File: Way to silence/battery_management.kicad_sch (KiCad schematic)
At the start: 9 parts, among them U2 SM5308

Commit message: [DRC] Working on BMS Sheet
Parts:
- added C10: C, symbol Way to silence:C
- added C11, C12, C13, C15, C16: 22uF, symbol Way to silence:C
- added C14: 4.7nF, symbol Way to silence:C
- added C9: 10uF, symbol Way to silence:C
- added L1: 1UH, symbol Way to silence:L
- added R16: 0.5R, symbol Way to silence:R
- added R17: 1R, symbol Way to silence:R
- added R18: 0.1R, symbol Way to silence:R
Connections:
- net GND: now also C10.2, C11.2, C12.2, C13.2, C14.2, C15.1, C16.1, C9.2
- net VIN: now reaches U2.1 (VIN)
- net VIN: now also C9.1, R16.1
- net at U2.6 (BAT): now also C16.2, R18.1
- net at U2.7 (SW): now also L1.1, R17.1
- net VOUT: now reaches U2.8 (VOUT)
- net VOUT: now also C11.1, C12.1, C13.1
- new net: C14.1, R17.2
- new net: C10.1, R16.2
- new net BAT: C15.2, L1.2, R18.2
- no-connect marks 0 -> 1

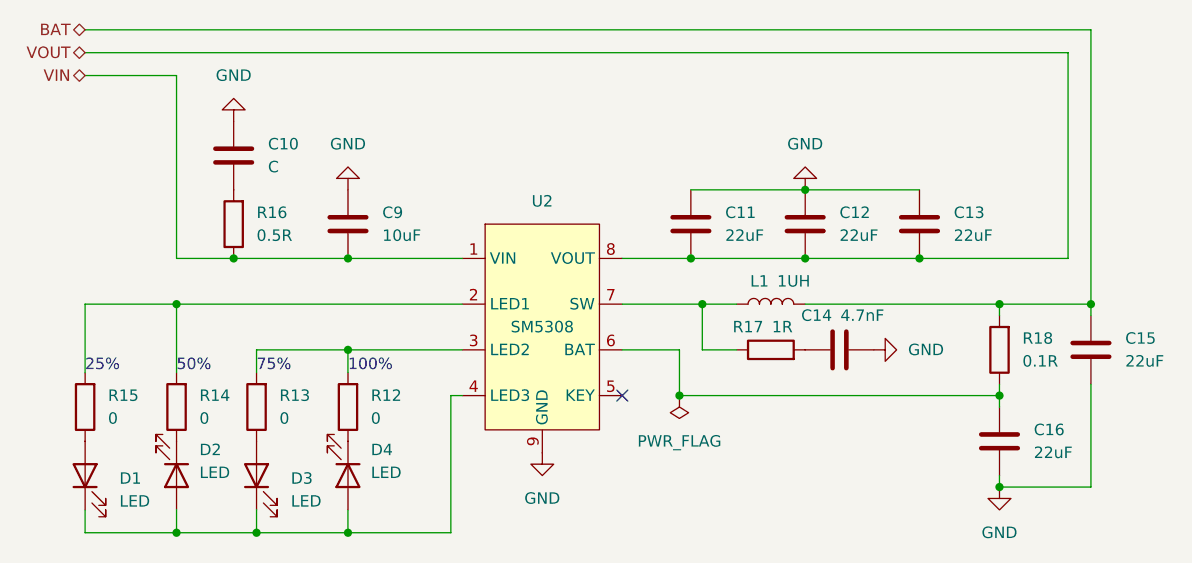
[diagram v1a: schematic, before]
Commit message: [ADD] LSCS Parts and Footprints for BMS
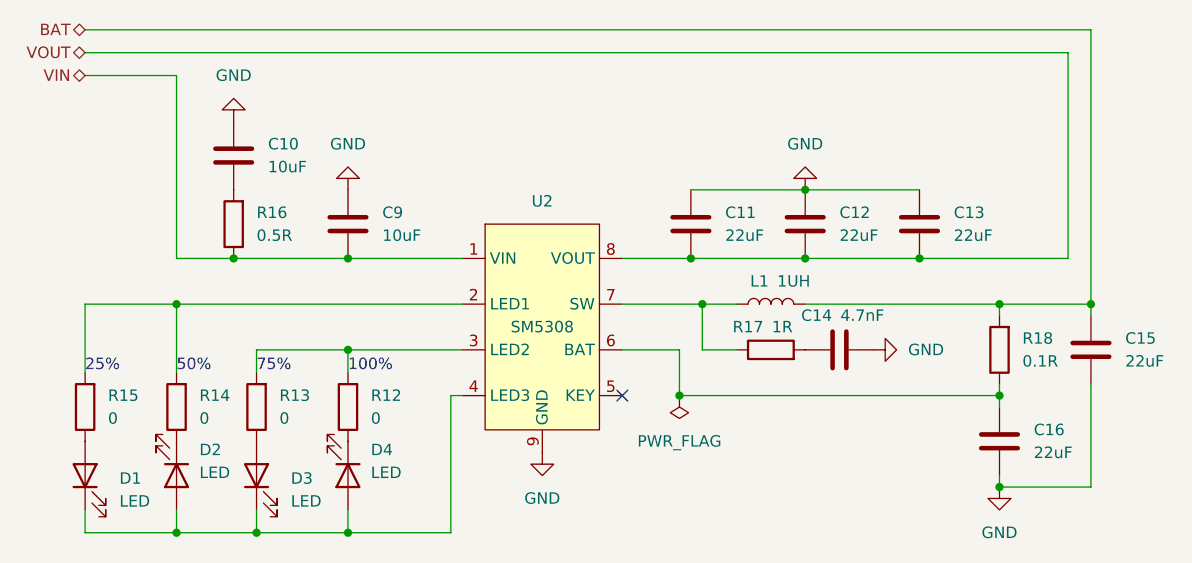
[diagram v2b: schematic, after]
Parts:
- C10: value C -> 10uF; footprint (none) -> Way to silence:C_0603_1608Metric; LCSC (none) -> C77041
- C11, C12, C13, C15, C16: footprint (none) -> Way to silence:C_0603_1608Metric; LCSC (none) -> C59461
- C14: footprint (none) -> Way to silence:C_0603_1608Metric
- C9: footprint (none) -> Way to silence:C_0603_1608Metric; LCSC (none) -> C77041
- D1, D2, D3, D4: footprint (none) -> Way to silence:LED_0603; LCSC (none) -> C84263
- R12, R13, R14, R15: footprint (none) -> Way to silence:R_0603_1608Metric; LCSC (none) -> C21189
- R16: footprint (none) -> Way to silence:R_0603_1608Metric; LCSC (none) -> C2934253
- R17: footprint (none) -> Way to silence:R_0603_1608Metric; LCSC (none) -> C25212
- R18: footprint (none) -> Way to silence:R_0603_1608Metric; LCSC (none) -> C705486
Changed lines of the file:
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@@
       (effects (font (size 1.27 1.27)) (justify right))
     )
-    (property "Footprint" "" (at 27.178 59.69 0)
+    (property "Footprint" "Way to silence:R_0603_1608Metric" (at 27.178 59.69 0)
       (effects (font (size 1.27 1.27)) hide)
     )
     (property "Datasheet" "~" (at 25.4 59.69 90)
+      (effects (font (size 1.27 1.27)) hide)
+    )
+    (property "LCSC" "C21189" (at 25.4 59.69 90)
       (effects (font (size 1.27 1.27)) hide)
     )
@@
       (effects (font (size 1.27 1.27)))
     )
-    (property "Footprint" "" (at 113.03 52.3748 90)
+    (property "Footprint" "Way to silence:C_0603_1608Metric" (at 113.03 52.3748 90)
       (effects (font (size 1.27 1.27)) hide)
     )
@@
       (effects (font (size 1.27 1.27)) (justify right))
     )
-    (property "Footprint" "" (at 104.4448 35.56 90)
+    (property "Footprint" "Way to silence:C_0603_1608Metric" (at 104.4448 35.56 90)
       (effects (font (size 1.27 1.27)) hide)
     )
@@
       (effects (font (size 1.27 1.27)) hide)
     )
+    (property "LCSC" "C59461" (at 105.41 39.37 90)
+      (effects (font (size 1.27 1.27)) hide)
+    )
     (pin "1")
     (pin "2")
@@
       (effects (font (size 1.27 1.27)) (justify right))
     )
-    (property "Footprint" "" (at 126.0348 59.69 90)
+    (property "Footprint" "Way to silence:C_0603_1608Metric" (at 126.0348 59.69 90)
       (effects (font (size 1.27 1.27)) hide)
     )
@@
       (effects (font (size 1.27 1.27)) hide)
     )
+    (property "LCSC" "C59461" (at 127 63.5 90)
+      (effects (font (size 1.27 1.27)) hide)
+    )
     (pin "1")
     (pin "2")
@@
       (effects (font (size 1.27 1.27)) (justify right))
     )
-    (property "Footprint" "" (at 37.338 59.69 0)
+    (property "Footprint" "Way to silence:R_0603_1608Metric" (at 37.338 59.69 0)
       (effects (font (size 1.27 1.27)) hide)
     )
@@
       (effects (font (size 1.27 1.27)) hide)
     )
+    (property "LCSC" "C21189" (at 35.56 59.69 90)
+      (effects (font (size 1.27 1.27)) hide)
+    )
     (pin "1")
     (pin "2")
@@
       (effects (font (size 1.27 1.27)) (justify right))
     )
-    (property "Footprint" "" (at 53.6448 35.56 90)
+    (property "Footprint" "Way to silence:C_0603_1608Metric" (at 53.6448 35.56 90)
       (effects (font (size 1.27 1.27)) hide)
     )
@@
       (effects (font (size 1.27 1.27)) hide)
     )
+    (property "LCSC" "C77041" (at 54.61 39.37 90)
+      (effects (font (size 1.27 1.27)) hide)
+    )
     (pin "1")
     (pin "2")
@@
       (effects (font (size 1.27 1.27)) (justify right))
     )
-    (property "Footprint" "" (at 25.4 67.31 0)
+    (property "Footprint" "Way to silence:LED_0603" (at 25.4 67.31 0)
       (effects (font (size 1.27 1.27)) hide)
     )
@@
       (effects (font (size 1.27 1.27)) hide)
     )
+    (property "LCSC" "C84263" (at 20.32 67.31 0)
+      (effects (font (size 1.27 1.27)) hide)
+    )
     (pin "1")
     (pin "2")
@@
       (effects (font (size 1.27 1.27)) (justify right))
     )
-    (property "Value" "C" (at 45.72 33.02 90)
-      (effects (font (size 1.27 1.27)) (justify right))
-    )
-    (property "Footprint" "" (at 40.9448 27.94 90)
+    (property "Value" "10uF" (at 45.72 33.02 90)
+      (effects (font (size 1.27 1.27)) (justify right))
+    )
+    (property "Footprint" "Way to silence:C_0603_1608Metric" (at 40.9448 27.94 90)
       (effects (font (size 1.27 1.27)) hide)
     )
     (property "Datasheet" "~" (at 41.91 31.75 90)
+      (effects (font (size 1.27 1.27)) hide)
+    )
+    (property "LCSC" "C77041" (at 41.91 31.75 90)
       (effects (font (size 1.27 1.27)) hide)
     )
@@
       (effects (font (size 1.27 1.27)) (justify right))
     )
-    (property "Footprint" "" (at 136.1948 49.53 90)
+    (property "Footprint" "Way to silence:C_0603_1608Metric" (at 136.1948 49.53 90)
       (effects (font (size 1.27 1.27)) hide)
     )
@@
       (effects (font (size 1.27 1.27)) hide)
     )
+    (property "LCSC" "C59461" (at 137.16 53.34 90)
+      (effects (font (size 1.27 1.27)) hide)
+    )
     (pin "1")
     (pin "2")
@@
       (effects (font (size 1.27 1.27)) (justify right))
     )
-    (property "Footprint" "" (at 56.388 59.69 0)
+    (property "Footprint" "Way to silence:R_0603_1608Metric" (at 56.388 59.69 0)
       (effects (font (size 1.27 1.27)) hide)
     )
@@
       (effects (font (size 1.27 1.27)) hide)
     )
+    (property "LCSC" "C21189" (at 54.61 59.69 90)
+      (effects (font (size 1.27 1.27)) hide)
+    )
     (pin "1")
     (pin "2")
@@
       (effects (font (size 1.27 1.27)) (justify right))
     )
-    (property "Footprint" "" (at 117.1448 35.56 90)
+    (property "Footprint" "Way to silence:C_0603_1608Metric" (at 117.1448 35.56 90)
       (effects (font (size 1.27 1.27)) hide)
     )
     (property "Datasheet" "~" (at 118.11 39.37 90)
+      (effects (font (size 1.27 1.27)) hide)
+    )
+    (property "LCSC" "C59461" (at 118.11 39.37 90)
       (effects (font (size 1.27 1.27)) hide)
     )
@@
       (effects (font (size 1.27 1.27)) (justify right))
     )
-    (property "Footprint" "" (at 128.778 53.34 0)
+    (property "Footprint" "Way to silence:R_0603_1608Metric" (at 128.778 53.34 0)
       (effects (font (size 1.27 1.27)) hide)
     )
     (property "Datasheet" "~" (at 127 53.34 90)
+      (effects (font (size 1.27 1.27)) hide)
+    )
+    (property "LCSC" "C705486" (at 127 53.34 90)
       (effects (font (size 1.27 1.27)) hide)
     )
@@
       (effects (font (size 1.27 1.27)) (justify left))
     )
-    (property "Footprint" "" (at 35.56 67.31 0)
+    (property "Footprint" "Way to silence:LED_0603" (at 35.56 67.31 0)
       (effects (font (size 1.27 1.27)) hide)
     )
@@
       (effects (font (size 1.27 1.27)) hide)
     )
+    (property "LCSC" "C84263" (at 40.64 67.31 0)
+      (effects (font (size 1.27 1.27)) hide)
+    )
     (pin "1")
     (pin "2")
@@
       (effects (font (size 1.27 1.27)) (justify right))
     )
-    (property "Footprint" "" (at 46.228 59.69 0)
+    (property "Footprint" "Way to silence:R_0603_1608Metric" (at 46.228 59.69 0)
       (effects (font (size 1.27 1.27)) hide)
     )
@@
       (effects (font (size 1.27 1.27)) hide)
     )
+    (property "LCSC" "C21189" (at 44.45 59.69 90)
+      (effects (font (size 1.27 1.27)) hide)
+    )
     (pin "1")
     (pin "2")
@@
       (effects (font (size 1.27 1.27)) (justify right))
     )
-    (property "Footprint" "" (at 44.45 67.31 0)
+    (property "Footprint" "Way to silence:LED_0603" (at 44.45 67.31 0)
       (effects (font (size 1.27 1.27)) hide)
     )
     (property "Datasheet" "~" (at 44.45 67.31 0)
+      (effects (font (size 1.27 1.27)) hide)
+    )
+    (property "LCSC" "C84263" (at 39.37 67.31 0)
       (effects (font (size 1.27 1.27)) hide)
     )
@@
       (effects (font (size 1.27 1.27)) (justify left))
     )
-    (property "Footprint" "" (at 54.61 67.31 0)
+    (property "Footprint" "Way to silence:LED_0603" (at 54.61 67.31 0)
       (effects (font (size 1.27 1.27)) hide)
     )
@@
       (effects (font (size 1.27 1.27)) hide)
     )
+    (property "LCSC" "C84263" (at 59.69 67.31 0)
+      (effects (font (size 1.27 1.27)) hide)
+    )
     (pin "1")
     (pin "2")
@@
       (effects (font (size 1.27 1.27)) (justify right))
     )
-    (property "Footprint" "" (at 43.688 39.37 0)
+    (property "Footprint" "Way to silence:R_0603_1608Metric" (at 43.688 39.37 0)
       (effects (font (size 1.27 1.27)) hide)
     )
@@
       (effects (font (size 1.27 1.27)) hide)
     )
+    (property "LCSC" "C2934253" (at 41.91 39.37 90)
+      (effects (font (size 1.27 1.27)) hide)
+    )
     (pin "1")
     (pin "2")
@@
       (effects (font (size 1.27 1.27)) (justify right))
     )
-    (property "Footprint" "" (at 91.7448 35.56 90)
+    (property "Footprint" "Way to silence:C_0603_1608Metric" (at 91.7448 35.56 90)
       (effects (font (size 1.27 1.27)) hide)
     )
     (property "Datasheet" "~" (at 92.71 39.37 90)
+      (effects (font (size 1.27 1.27)) hide)
+    )
+    (property "LCSC" "C59461" (at 92.71 39.37 90)
       (effects (font (size 1.27 1.27)) hide)
     )
@@
       (effects (font (size 1.27 1.27)))
     )
-    (property "Footprint" "" (at 101.6 55.118 0)
+    (property "Footprint" "Way to silence:R_0603_1608Metric" (at 101.6 55.118 0)
       (effects (font (size 1.27 1.27)) hide)
     )
@@
       (effects (font (size 1.27 1.27)) hide)
     )
+    (property "LCSC" "C25212" (at 101.6 53.34 0)
+      (effects (font (size 1.27 1.27)) hide)
+    )

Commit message: [ADD] References in readme
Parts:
- C14: LCSC (none) -> C53987
- R18: LCSC C705486 -> C111027
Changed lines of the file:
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@@
+      (effects (font (size 1.27 1.27)) hide)
+    )
+    (property "LCSC" "C53987" (at 109.22 53.34 0)
       (effects (font (size 1.27 1.27)) hide)
     )
@@
       (effects (font (size 1.27 1.27)) hide)
     )
-    (property "LCSC" "C705486" (at 127 53.34 90)
-      (effects (font (size 1.27 1.27)) hide)
-    )
+    (property "LCSC" "C111027" (at 127 53.34 90)
+      (effects (font (size 1.27 1.27)) hide)
+    )

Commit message: [ADD] Inductor references
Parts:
- L1: footprint (none) -> Way to silence:Inductor; LCSC (none) -> C2847468
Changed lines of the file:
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@@
       (effects (font (size 1.27 1.27)))
     )
-    (property "Footprint" "" (at 101.6 48.26 90)
+    (property "Footprint" "Way to silence:Inductor" (at 101.6 48.26 90)
       (effects (font (size 1.27 1.27)) hide)
     )
@@
       (effects (font (size 1.27 1.27)) hide)
     )
+    (property "LCSC" "C2847468" (at 101.6 40.64 0)
+      (effects (font (size 1.27 1.27)) hide)
+    )

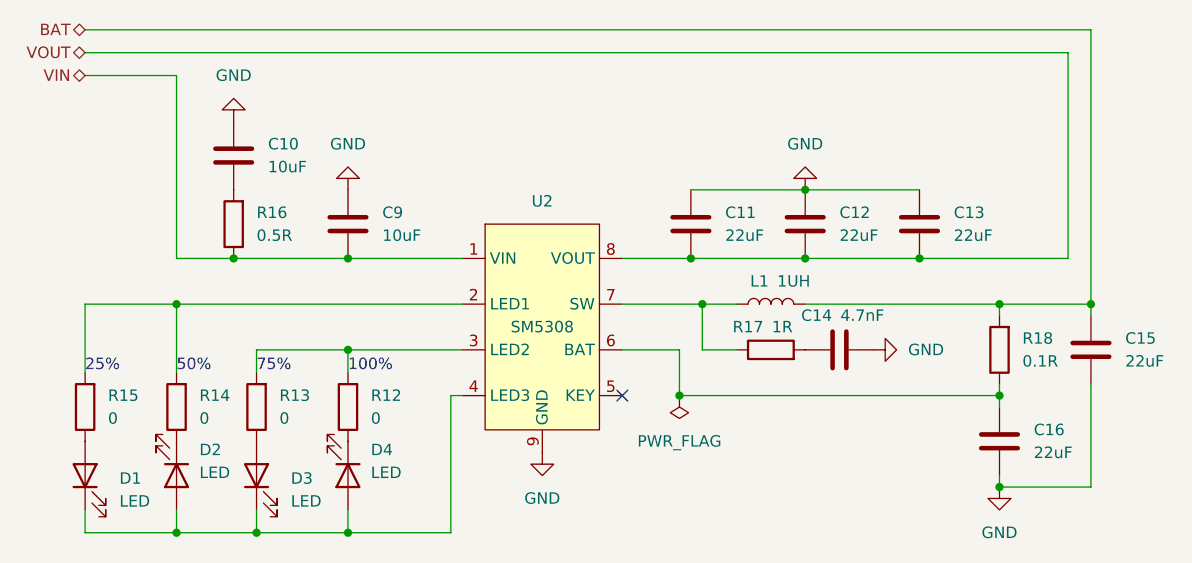
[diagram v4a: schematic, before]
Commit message: [ADD] Styles to shematics
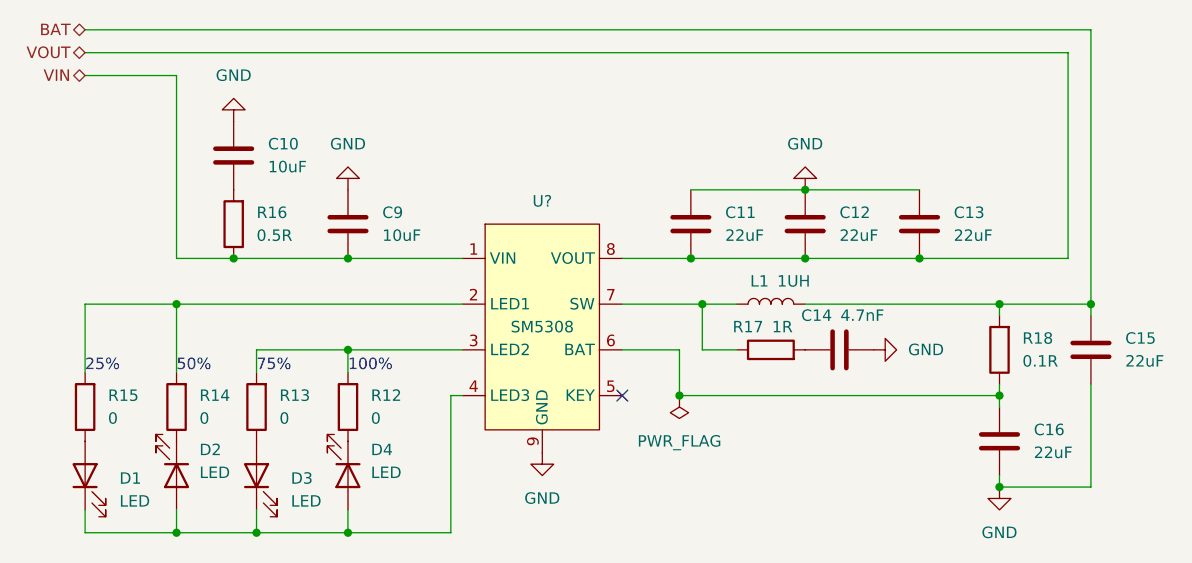
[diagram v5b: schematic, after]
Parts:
- renumbered U2 to U?
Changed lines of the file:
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@@
   (symbol (lib_id "Way to silence:SM5308") (at 76.2 50.8 0) (unit 1)
     (in_bom yes) (on_board yes) (dnp no) (fields_autoplaced)
-    (property "Reference" "U2" (at 76.2 36.83 0)
+    (property "Reference" "U?" (at 76.2 36.83 0)
       (effects (font (size 1.27 1.27)))
     )
@@
       (project "Way to silence"
         (path "/9822a1be-a034-44c3-8530-56368958b215"
-          (reference "U2") (unit 1)
+          (reference "U?") (unit 1)
         )
         (path "/9822a1be-a034-44c3-8530-56368958b215/be1db4b6-aade-41cb-8a40-ce07da27a5fd"

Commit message: [ADD] Shematics files settings
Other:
- title: (none) -> Battery Management
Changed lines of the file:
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@@
 (kicad_sch (version 20230121) (generator eeschema)
-  (paper "A4")
+  (paper "A5")
+  (title_block
+    (title "Battery Management")
+    (date "2023-10-10")
+    (rev "1.0")
+  )
   (junction (at 127 48.26) (diameter 0) (color 0 0 0 0)
   )

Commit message: [UDPT] Leds colors
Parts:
- D1, D2, D3, D4: LCSC C84263 -> C84268
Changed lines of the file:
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@@
       (effects (font (size 1.27 1.27)) hide)
     )
-    (property "LCSC" "C84263" (at 20.32 67.31 0)
+    (property "LCSC" "C84268" (at 20.32 67.31 0)
       (effects (font (size 1.27 1.27)) hide)
     )
@@
       (effects (font (size 1.27 1.27)) hide)
     )
-    (property "LCSC" "C84263" (at 40.64 67.31 0)
+    (property "LCSC" "C84268" (at 40.64 67.31 0)
       (effects (font (size 1.27 1.27)) hide)
     )
@@
       (effects (font (size 1.27 1.27)) hide)
     )
-    (property "LCSC" "C84263" (at 39.37 67.31 0)
+    (property "LCSC" "C84268" (at 39.37 67.31 0)
       (effects (font (size 1.27 1.27)) hide)
     )
@@
       (effects (font (size 1.27 1.27)) hide)
     )
-    (property "LCSC" "C84263" (at 59.69 67.31 0)
-      (effects (font (size 1.27 1.27)) hide)
-    )
+    (property "LCSC" "C84268" (at 59.69 67.31 0)
+      (effects (font (size 1.27 1.27)) hide)
+    )

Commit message: [UDPT] Sheet name
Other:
- title: Battery Management -> Battery Management System
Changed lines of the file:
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@@
   (paper "A5")
   (title_block
-    (title "Battery Management")
+    (title "Battery Management System")
     (date "2023-10-10")
     (rev "1.0")
